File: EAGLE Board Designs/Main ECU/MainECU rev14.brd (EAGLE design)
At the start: 109.2 x 115.6 mm, 331 parts, among them J1 CONNECTOR-34__, J2 CONNECTOR-34__, J3 ADIS16460, K1 RELAY_DPDT_07DSMT, K2 RELAY_DPDT_07DSMT, K3 RELAY_DPDT_07DSMT, K4 RELAY_DPDT_07DSMT, K5 RELAY_DPDT_07DSMT, Q1 TRANSISTOR_N_MOS__DMG3406L-7, Q2 TRANSISTOR_P_MOS_SOT-23_DMP30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, Q3 TRANSISTOR_P_MOS_SOT-23_DMP30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, Q4 TRANSISTOR_N_MOS__DMG3406L-7, U1 MAX7400, U10 MCP3208, U11 MCP3208, U12 TCAN1051HQV-Q1, U13 TCAN1051HQV-Q1, U14 MCP3208, U15 OPAMP_1_CHANNEL_OPA991, U16 LOGICGATE_OR, U17 OPAMP_1_CHANNEL_OPA991, U18 LOGICGATE_OR, U19 OPAMP_1_CHANNEL_OPA991, U2 MAX7400, U20 LOGICGATE_OR, U21 LOGICGATE_OR, U22 OPAMP_1_CHANNEL_OPA991, U23 LOGICGATE_NOR, U24 LOGICGATE_OR, U25 OPAMP_1_CHANNEL_OPA991, U26 OPAMP_1_CHANNEL_OPA991, U27 OPAMP_1_CHANNEL_OPA991, U28 LOGICGATE_AND_DCK3, U29 OPAMP_1_CHANNEL_OPA991, U3 MAX7400, U30 OPAMP_1_CHANNEL_OPA991, U31 TCAN1051HQV-Q1, U32 TCAN1051HQV-Q1, U33 TCAN1051HQV-Q1, U34 TCAN1051HQV-Q1, U35 MAX7400, U36 MAX7400, U37 ADM8316WBX30, U38 MAX7400, U4 MAX7400, U5 VOLTAGE_REGULATOR_SOT-223_3.3V, U6 MAX7400, U7 MAX7400, U8 MAX7400, U9 MAX7400

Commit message: routing progress
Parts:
- removed C45, C49: CAPACITOR_0603_10V_0.1UF, HyTechDevices:0603-CAP
- removed C46, C47: CAPACITOR_0603_10V_1UF, HyTechDevices:0603-CAP
- removed D22: TVS__5V, HyTechDevices:SOT-23
- removed R47: RESISTOR_0603_10K, HyTechDevices:0603-RES
- removed R48: RESISTOR_0603_2.55K, HyTechDevices:0603-RES
- removed U14: MCP3208, Temp:SOIC-16
- moved $$U$1 91.5 mm to (33.0, 30.2)
- moved TP7 86.6 mm to (-7.37, 43.4)
- moved TP8 86.4 mm to (-12.2, 43.4)
- moved D5 49.2 mm to (63.0, 80.3), flipped to the bottom, turned to 90 degrees
- moved R1 46.3 mm to (63.0, 82.8), flipped to the bottom, turned to 180 degrees
- moved R2 44.6 mm to (63.0, 84.3), flipped to the bottom, turned to 0 degrees
- moved TP3 31.8 mm to (-7.37, 53.1)
- moved TP4 31.8 mm to (-12.4, 53.1)
- moved TP6 31.8 mm to (-12.2, 49.3)
- moved TP5 31.8 mm to (-7.11, 49.3)
- moved R34 2.62 mm to (75.7, 93.7), turned to 90 degrees
- moved R51 0.25 mm to (35.6, 54.4)
- moved R55 0.25 mm to (25.9, 54.4)
- moved R58 0.25 mm to (16.3, 54.4)
- moved C56 0.25 mm to (15.5, 52.1)
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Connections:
- removed net !AD4_CS: A3.D33, U14.10
- removed net 24V_SENSE_TCU: D22.3, R47.1, R48.2, U14.1
- removed net N$34: U14.9
- removed net N$39: U14.16
- net +24V: no longer R47.2
- net +3V3: no longer C47.1, C49.1, U14.15
- net +5V: no longer C45.1, C46.1
- net 24V_SENSE_ECU: now also A3.D26
- net CURRENT: now also A3.D39; no longer U14.2
- net GND: no longer C45.2, C46.2, C47.2, C49.2, D22.1, R48.1, U14.14
- net REFERENCE: now also A3.D38; no longer U14.3
- net TELEM_CLK: no longer U14.13
- net TELEM_SDI: no longer U14.12
- net TELEM_SDO: no longer U14.11
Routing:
- net +5V: track 205.5 -> 369.6 mm, vias 8 -> 10
- net 24V_SENSE_ECU: track 4.93 -> 101.2 mm, vias 0 -> 2
- net +3V3: track 53.0 -> 142.0 mm, vias 4 -> 6
- net CURRENT: track 21.6 -> 93.9 mm, vias 0 -> 3
- net REFERENCE: track 6.51 -> 78.5 mm, vias 0 -> 3
- net SHDN_G: track 5.76 -> 77.7 mm
- net CANL_1: track 38.2 -> 106.2 mm
- net CANH_1: track 37.8 -> 105.3 mm
- net CANL_2: track 28.6 -> 93.0 mm
- net CANH_2: track 26.6 -> 90.4 mm
- net ECU_SDO: track 66.7 -> 128.0 mm, vias 0 -> 2
- net ECU_SDI: track 64.0 -> 121.3 mm, vias 0 -> 2
- net ECU_CLK: track 67.7 -> 124.4 mm, vias 0 -> 2
- net VBAT: track 0.00 -> 40.2 mm
- net BRAKE_1: track 9.56 -> 38.0 mm, vias 0 -> 2
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
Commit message: routing progress
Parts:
- moved R52 14.9 mm to (39.4, 41.9), turned to 90 degrees
- moved C52 12.2 mm to (40.4, 39.6), turned to 180 degrees
- moved JP5 10.9 mm to (42.9, 41.9), turned to 0 degrees
- moved R49 8.32 mm to (43.4, 39.6), turned to 180 degrees
- moved LATCH 3.30 mm to (73.9, 93.7)
- moved R34 3.30 mm to (72.4, 93.7)
- moved R93 1.08 mm to (81.5, 85.1), turned to 90 degrees
- moved R64 1.02 mm to (13.7, 38.1)
- moved R65 1.02 mm to (12.2, 38.1)
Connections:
- new net STEERING_1_PRE: R41.2, R42.2, U8.2
- net SHDN_B_READ: now also A2.D24; no longer A2.D3
- net SHDN_C_READ: now also A2.D41; no longer A2.D4
- net SHDN_D_READ: now also A2.D40; no longer A2.D5
- net SHDN_E_READ: now also A2.D39; no longer A2.D6
- net STEERING_1_EXT: no longer R41.2, R42.2, U8.2
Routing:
- net +5V: track 369.6 -> 633.4 mm, vias 10 -> 33
- net BSPD_OK_LV: track 4.23 -> 102.3 mm, vias 0 -> 2
- net !IMU_CS: track 0.00 -> 78.5 mm
- net !IMU_RESET: track 0.00 -> 74.3 mm, vias 0 -> 2
- net IMU_SYNC: track 0.00 -> 65.6 mm
- net SOFTWARE_OK: track 1.61 -> 65.4 mm, vias 0 -> 3
- net ECU_CLK: track 124.4 -> 180.6 mm
- net IMU_DATAREADY: track 0.00 -> 55.4 mm, vias 0 -> 2
- net !AD2_CS: track 0.00 -> 54.4 mm, vias 0 -> 2
- net INERTIA_SENSE_EXT: track 3.21 -> 57.0 mm, vias 0 -> 1
- net +3V3: track 142.0 -> 195.6 mm, vias 6 -> 8
- net WATCHDOG: track 0.00 -> 51.6 mm, vias 0 -> 3
- net SHDN_E_READ: track 1.52 -> 48.5 mm, vias 0 -> 2
- net +24V: track 64.5 -> 110.2 mm, vias 0 -> 3
- net SHDN_C_READ: track 1.52 -> 44.3 mm, vias 0 -> 2
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- added copper zone on layer 15, net GND
- added copper zone on layer 16, net GND
- added copper zone on layer 2, net GND

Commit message: all routing except test points
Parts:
- moved C60 3.45 mm to (14.7, 20.6)
- moved C63 3.18 mm to (11.7, 20.6)
- moved C62 3.18 mm to (13.2, 20.6)
- moved C61 0.25 mm to (30.7, 52.1)
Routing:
- net +3V3: track 195.6 -> 241.1 mm, vias 8 -> 9
- net GND: track 0.00 -> 5.59 mm, vias 8 -> 34
- net BMS_OK: track 59.6 -> 60.6 mm
- net N$14: track 23.7 -> 22.7 mm
- net SHDN_G: track 77.7 -> 78.6 mm
- net SHDN_C: track 52.3 -> 51.5 mm
- net +5V: track 633.4 -> 633.9 mm

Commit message: passed DRC
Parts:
- removed $$U$4: (no value), HyTechManufacturing:LOGO_HYTECH_SQUARE_LARGE
- added TP10, TP9: TEST_POINT, HyTechDevices:5015
- added U$6: (no value), HyTechManufacturing:LOGO_HYTECH_MEDIUM
- moved TP4 55.7 mm to (42.4, 62.7)
- moved TP6 52.1 mm to (38.1, 62.7)
- moved TP3 50.1 mm to (42.4, 58.9)
- moved TP5 46.2 mm to (38.1, 58.9)
- moved TP8 33.1 mm to (17.0, 58.9)
- moved TP7 32.6 mm to (21.3, 58.9)
- moved $$U$1 8.42 mm to (41.4, 31.0)
- moved D12 0.25 mm to (86.1, 99.8)
- moved D4 0.25 mm to (86.1, 103.4)
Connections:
- net CURRENT: now also TP9.1
- net REFERENCE: now also TP10.1
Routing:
- net REFERENCE_OOR_LO: track 10.9 -> 31.9 mm, vias 0 -> 2
- net CURRENT_OOR_LO: track 7.08 -> 25.8 mm, vias 0 -> 2
- net CURRENT_OOR_HI: track 3.67 -> 19.8 mm, vias 0 -> 2
- net REFERENCE_OOR_HI: track 9.52 -> 24.3 mm, vias 0 -> 2
- net BRAKE_OOR_HI: track 17.0 -> 27.0 mm, vias 0 -> 2
- net REFERENCE: track 116.5 -> 126.2 mm
- net BRAKE_OOR_LO: track 12.9 -> 21.6 mm, vias 0 -> 2
- net CURRENT: track 129.5 -> 135.2 mm
- net +3V3: track 241.1 -> 241.9 mm
- net +5V: track 633.9 -> 633.2 mm

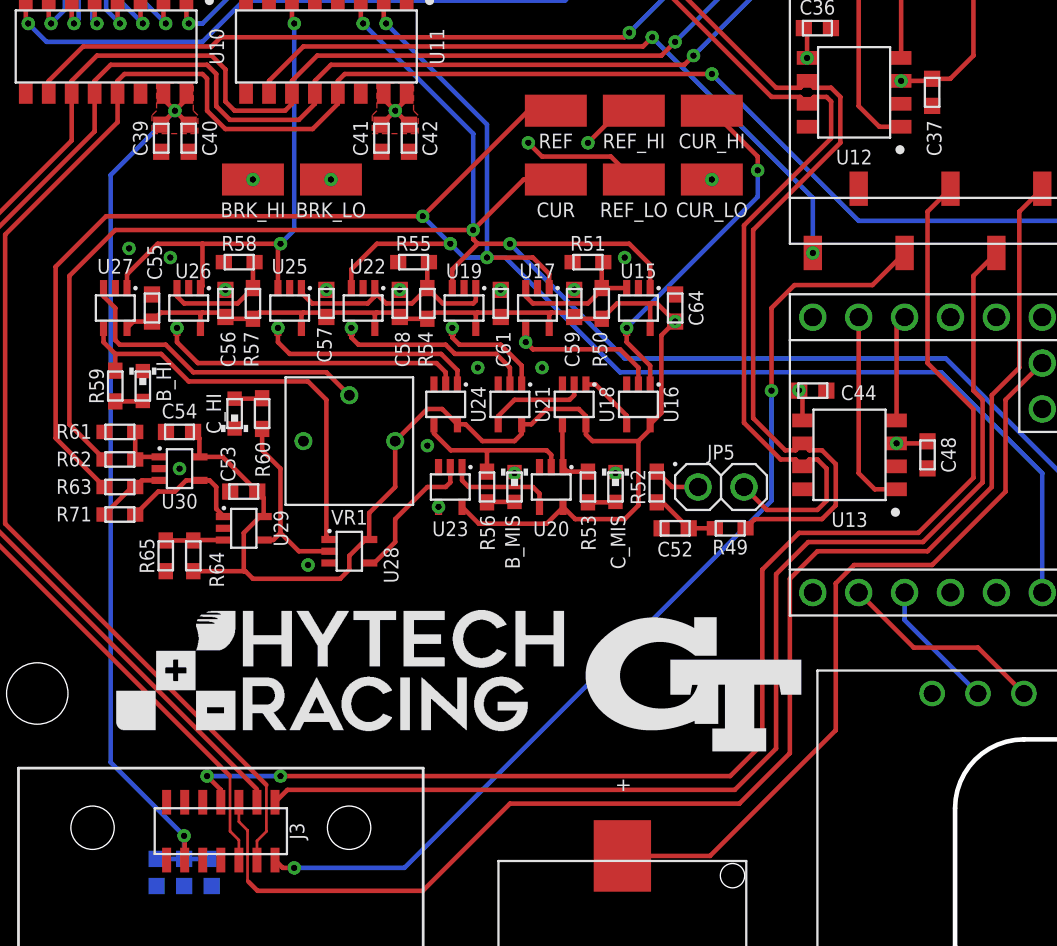
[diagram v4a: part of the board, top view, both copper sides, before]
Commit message: updated resistors. updated BSPD. passed DRC
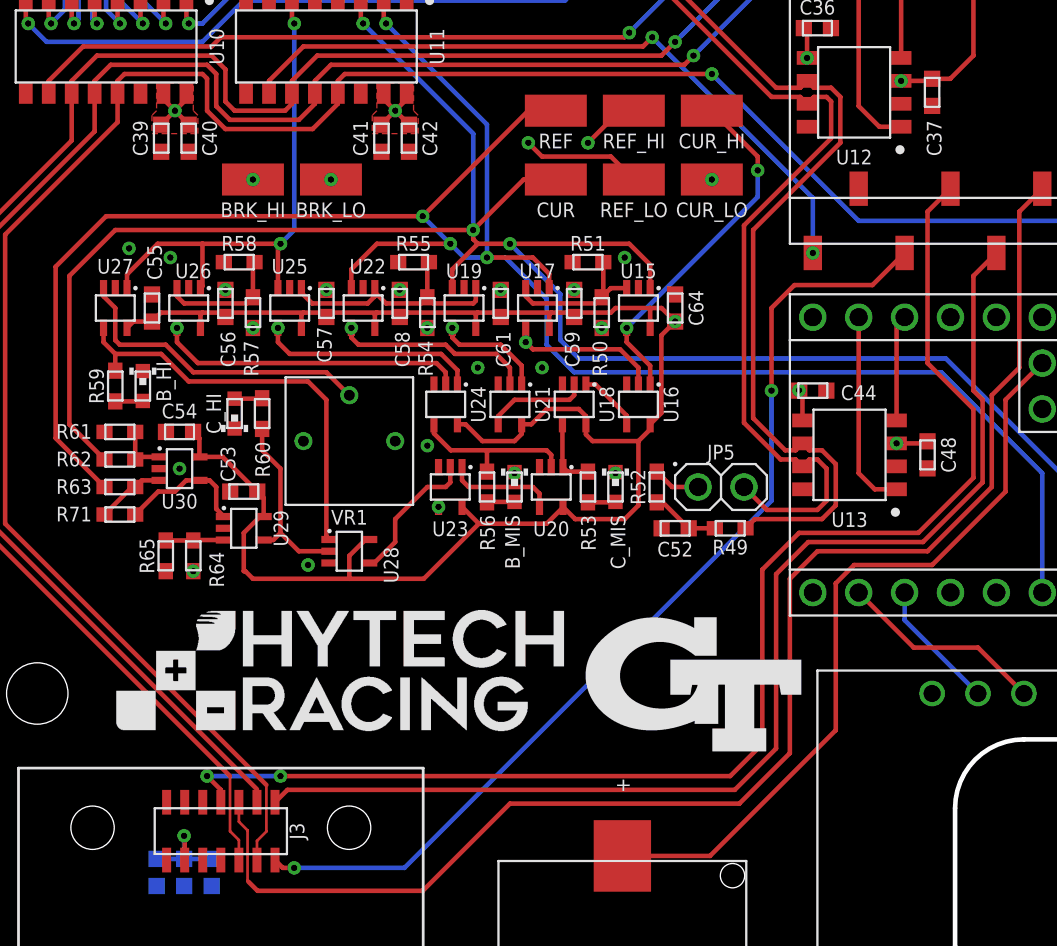
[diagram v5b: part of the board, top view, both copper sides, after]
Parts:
- R101, R75, R79, R83: value RESISTOR_0603_13K -> RESISTOR_0603_10K
- R64: value RESISTOR_0603_10K -> RESISTOR_0603_14K
- R74, R78, R82, R99: value RESISTOR_0603_3.3K -> RESISTOR_0603_1.24K
- moved R50 0.51 mm to (36.3, 51.6)
- moved R54 0.51 mm to (26.7, 51.6)
- moved R57 0.51 mm to (17.0, 51.6)
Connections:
- net 0V5 renamed 0V26
- net 4V5 renamed 2V38
- net 4V5_1 renamed 2V38_1
- net +3V3: now also R50.2, R54.2, R57.2, R64.2, VR1.3
- net +5V: no longer R50.2, R54.2, R57.2, R64.2, VR1.3
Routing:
- net +3V3: track 241.9 -> 278.2 mm, vias 9 -> 13
- net +5V: track 633.2 -> 627.9 mm
- net CURRENT: track 135.2 -> 136.7 mm
- net REFERENCE: track 126.2 -> 127.7 mm
- net BSPD_OK_LV: track 102.7 -> 103.4 mm

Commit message: design review changes
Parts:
- R1: value RESISTOR_0603_2.55K -> RESISTOR_0603_1.24K
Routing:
- net IMU_DATAREADY: track 55.4 -> 56.4 mm

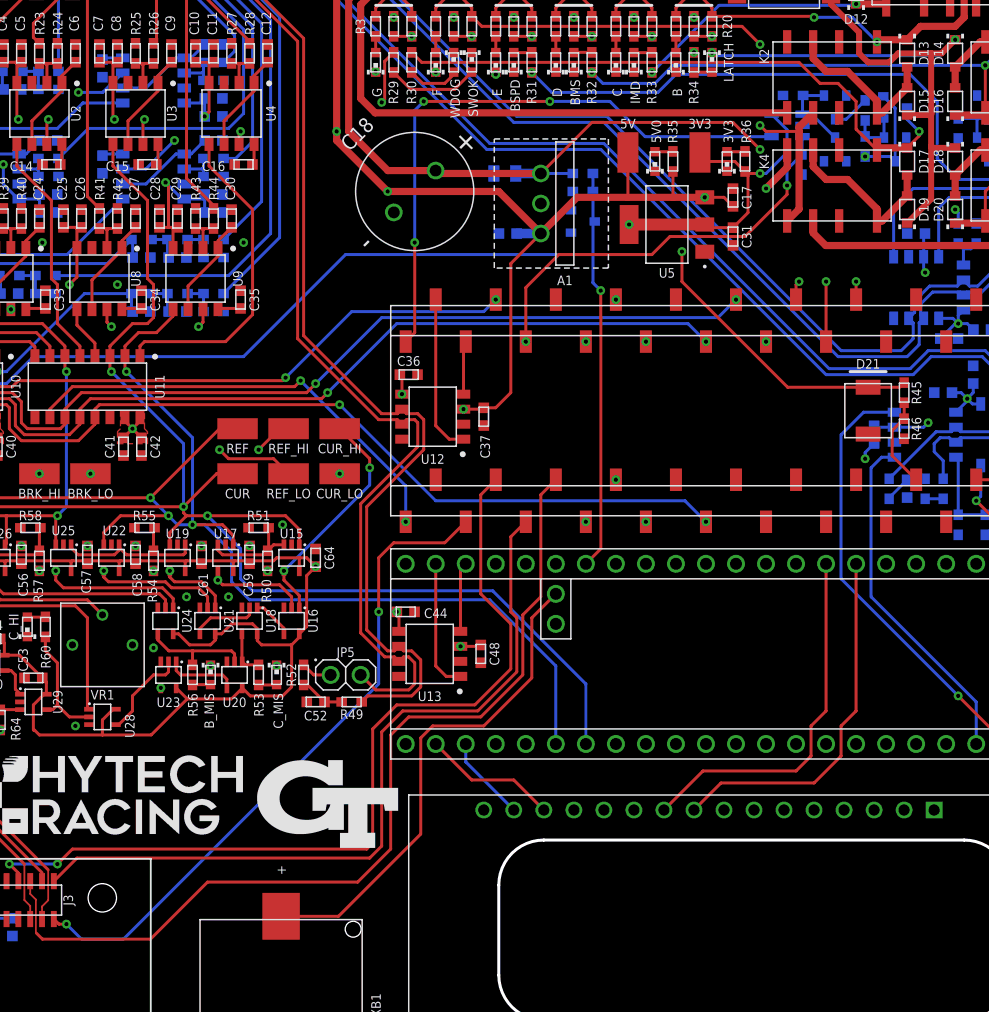
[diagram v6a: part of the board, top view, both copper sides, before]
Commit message: added ECU->TCU serial, AMS&IMD sense
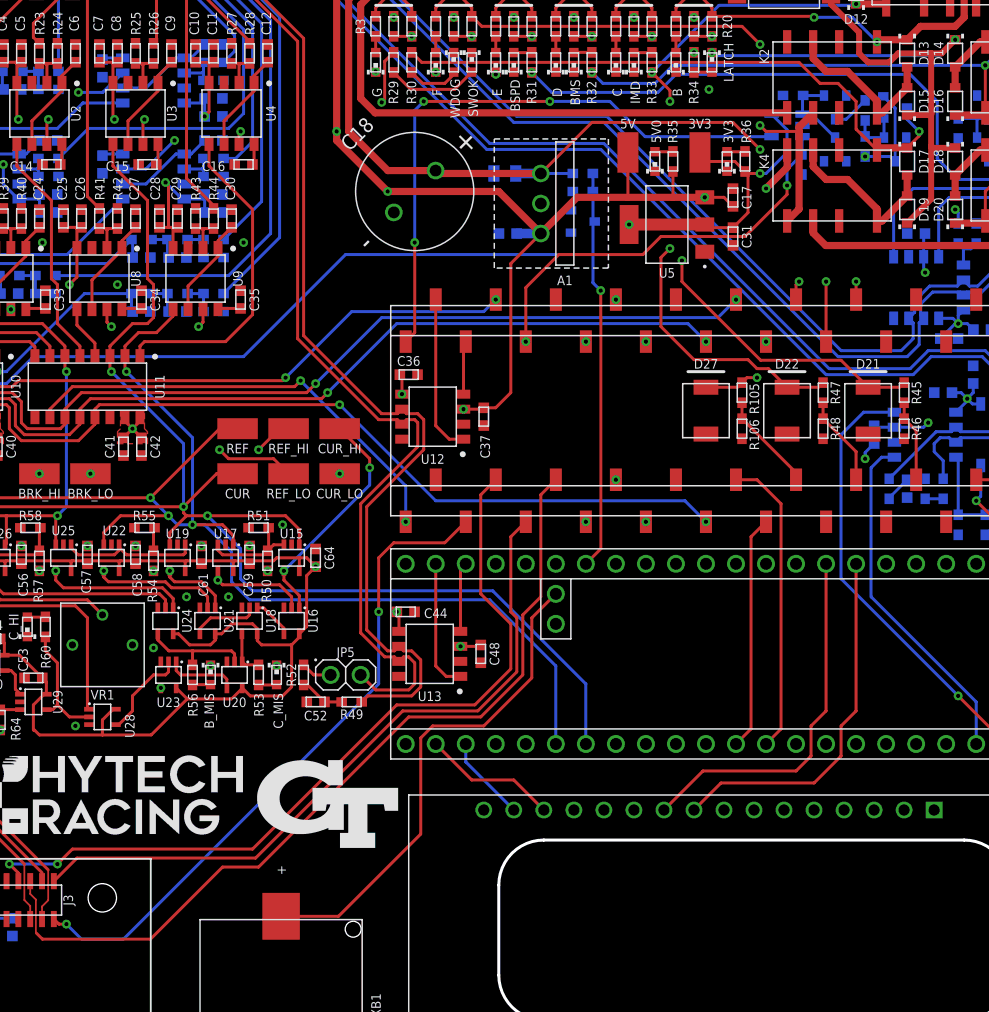
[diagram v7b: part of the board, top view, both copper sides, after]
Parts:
- added D22, D27: TVS_DO-214AA_28V, HyTechDevices:DO-214AA
- added R105, R47: RESISTOR_0603_36.5K, HyTechDevices:0603-RES
- added R106, R48: RESISTOR_0603_4.64K, HyTechDevices:0603-RES
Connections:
- removed net GPS_RX: A3.D14
- removed net GPS_TX: A3.D15
- new net BMS_OK_SENSE: A2.D16, R105.1, R106.2
- new net ECU_RX3: A2.D15, A3.D14
- new net ECU_TX3: A2.D14, A3.D15
- new net OKHS_SENSE: A2.D18, R47.1, R48.2
- net BMS_OK: now also D27.2, R105.2
- net GND: now also D22.1, D27.1, R106.1, R48.1
- net OKHS_IN: now also D22.2, R47.2
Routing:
- net BMS_OK: track 60.6 -> 100.6 mm, vias 2 -> 3
- net OKHS_IN: track 37.9 -> 76.3 mm, vias 3 -> 5
- net ECU_TX3: track 0.00 -> 25.5 mm
- net ECU_RX3: track 0.00 -> 19.8 mm
- net BMS_OK_SENSE: track 0.00 -> 8.41 mm
- net OKHS_SENSE: track 0.00 -> 7.67 mm
- net IMU_SYNC: track 65.6 -> 59.9 mm
- net !IMU_RESET: track 74.3 -> 68.6 mm
- net !IMU_CS: track 78.5 -> 72.9 mm
- net INERTIA_SENSE: track 7.78 -> 6.94 mm
- net BSPD_OK_LV: track 103.4 -> 104.2 mm
- net +3V3: track 278.2 -> 278.8 mm
- net +5V: track 627.9 -> 628.5 mm
- net GND: vias 34 -> 35

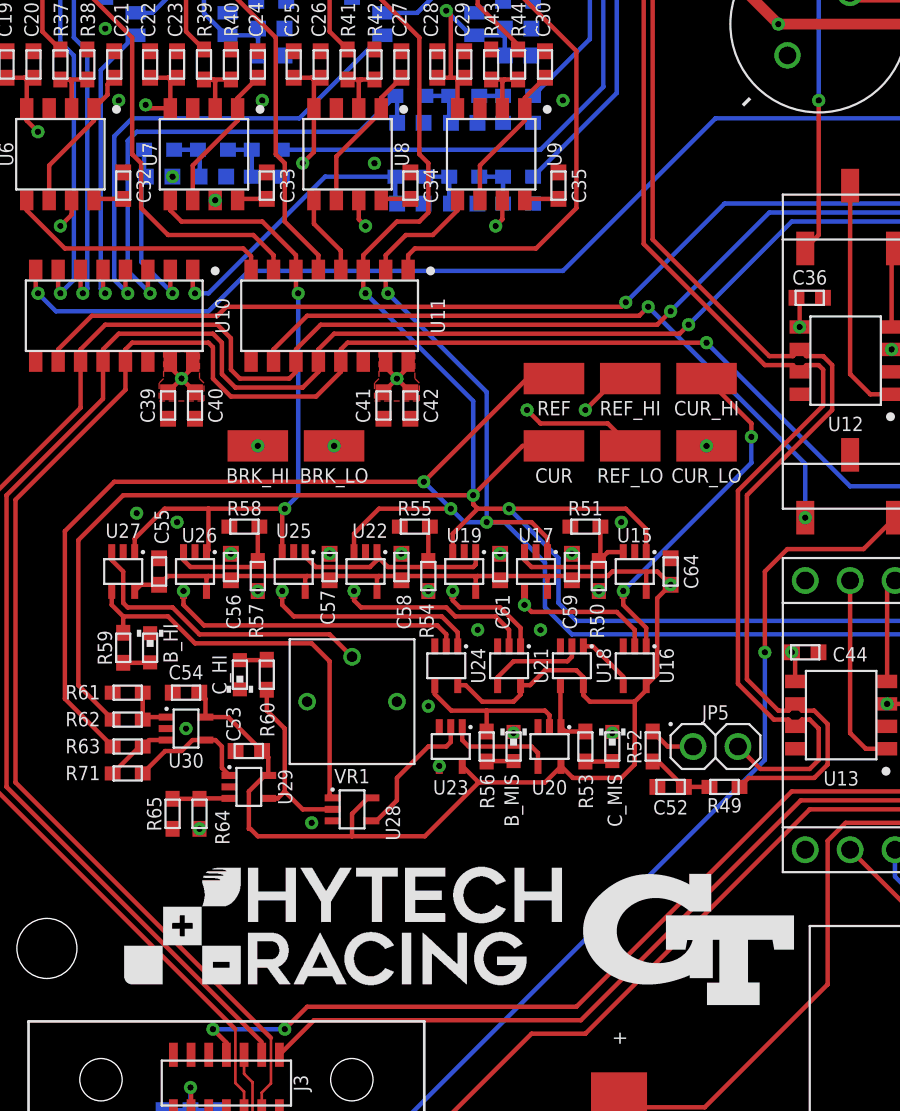
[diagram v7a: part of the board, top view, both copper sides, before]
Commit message: added selectable reference pot
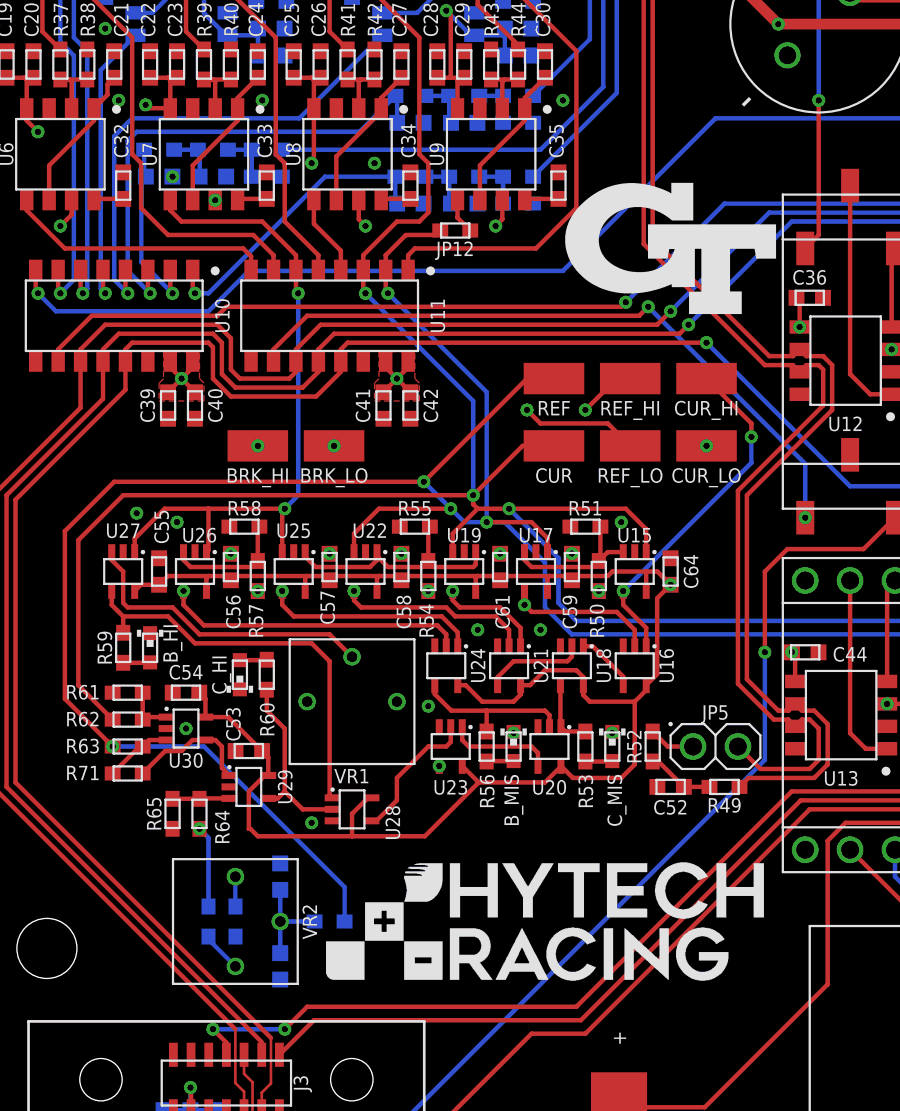
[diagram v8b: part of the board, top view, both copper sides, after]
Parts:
- added C45: CAPACITOR_0603_10V_0.1UF, HyTechDevices:0603-CAP
- added C46: CAPACITOR_0603_10V_1UF, HyTechDevices:0603-CAP
- added JP12: JUMPER_0603_, HyTechDevices:0603-RES
- added JP13: DNP, HyTechDevices:0603-RES
- added R107, R108: RESISTOR_0603_10K, HyTechDevices:0603-RES
- added VR2: RESISTOR_TRIMPOT_10K_3362P, HyTechDevices:3362P
- moved $$U$1 39.1 mm to (40.4, 70.1)
- moved U$6 11.4 mm to (20.8, 28.7)
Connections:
- new net N$34: JP12.2, U9.5
- new net N$39: R107.1, VR2.3
- new net N$46: C45.1, C46.1, JP13.1, VR2.2
- new net N$48: R108.2, VR2.1
- net +3V3: now also R107.2
- net GND: now also C45.2, C46.2, R108.1
- net REFERENCE: now also JP12.1, JP13.2; no longer U9.5
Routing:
- net REFERENCE: track 127.7 -> 144.1 mm, vias 4 -> 5
- net N$46: track 0.00 -> 5.52 mm
- net +3V3: track 278.8 -> 283.4 mm
- net N$39: track 0.00 -> 2.32 mm
- net N$34: track 0.00 -> 2.01 mm
- net N$48: track 0.00 -> 1.69 mm
